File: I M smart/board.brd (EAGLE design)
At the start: 20 x 100 mm, 26 parts, among them IC1 TL072P

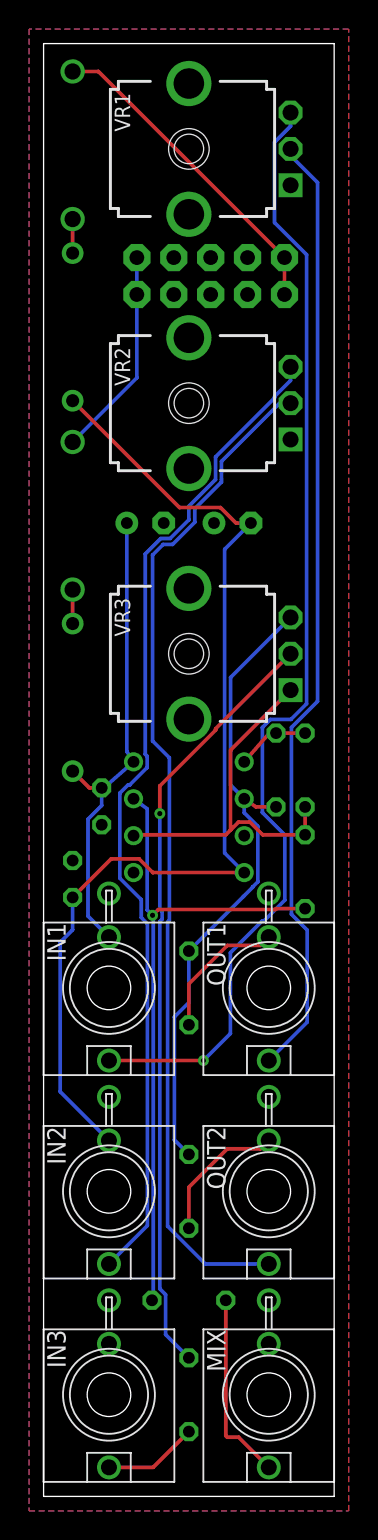
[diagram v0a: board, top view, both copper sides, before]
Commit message: Don't connect the power rails directly to output as it shorts the entire case if connected to GND!
Update I M smart to rev0.1. Compatible with panel.
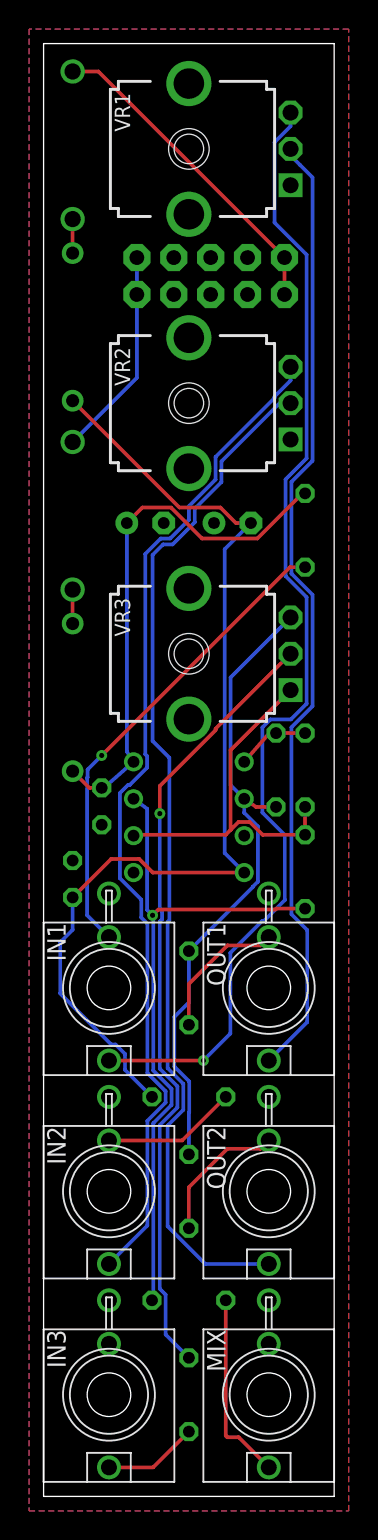
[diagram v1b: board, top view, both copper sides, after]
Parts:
- added R8, R9: 100K, rcl:0204/5
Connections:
- new net N$11: IN2.P$2, R9.1
- new net N$12: IN1.P$2, R8.1
- net +12V: now also R8.2; no longer IN1.P$2
- net -12V: now also R9.2; no longer IN2.P$2
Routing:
- net N$12: track 0.00 -> 32.9 mm, vias 0 -> 1
- net N$11: track 0.00 -> 9.28 mm
- net +12V: track 33.2 -> 36.8 mm
- net -12V: track 72.9 -> 71.3 mm
- net N$5: track 78.2 -> 79.4 mm
- net N$6: track 69.1 -> 70.1 mm
- net N$21: track 45.9 -> 46.9 mm
- net N$10: track 53.1 -> 54.2 mm
- net N$7: track 65.8 -> 66.7 mm
- net N$8: track 70.0 -> 70.9 mm
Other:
- board text added: "rev0.1"
- board text removed: "rev0"
